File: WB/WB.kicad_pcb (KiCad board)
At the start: 2 copper layers, 89.2 x 84.2 mm, 47 parts, among them J1 Conn_01x04, J2 Conn_01x04, J3 Conn_01x04, J4 Conn_01x04, J5 Pump, J6 Actuator, J7 Actuator, J8 Screw_Terminal_01x02, M1 Fan, Q1 Q_NMOS_GDS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

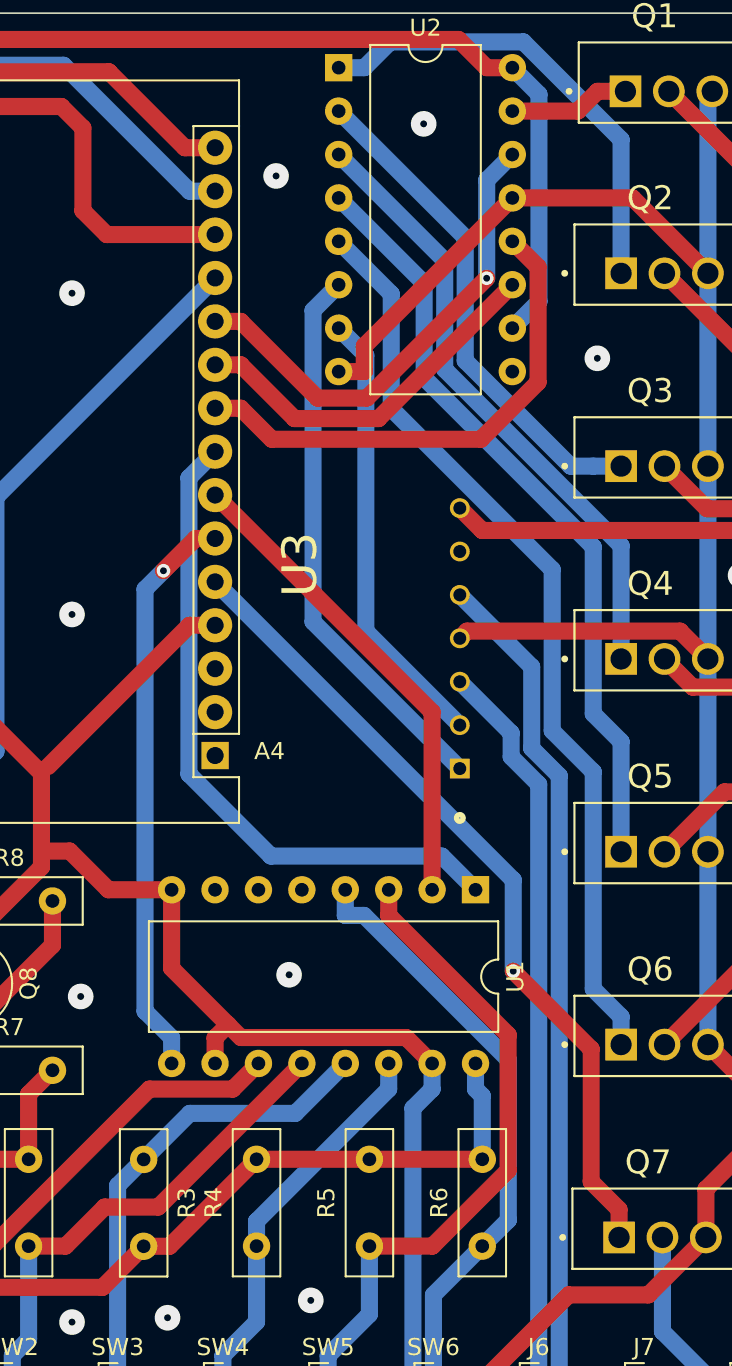
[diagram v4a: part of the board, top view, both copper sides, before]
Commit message: 配線がかぶっていたところを修正
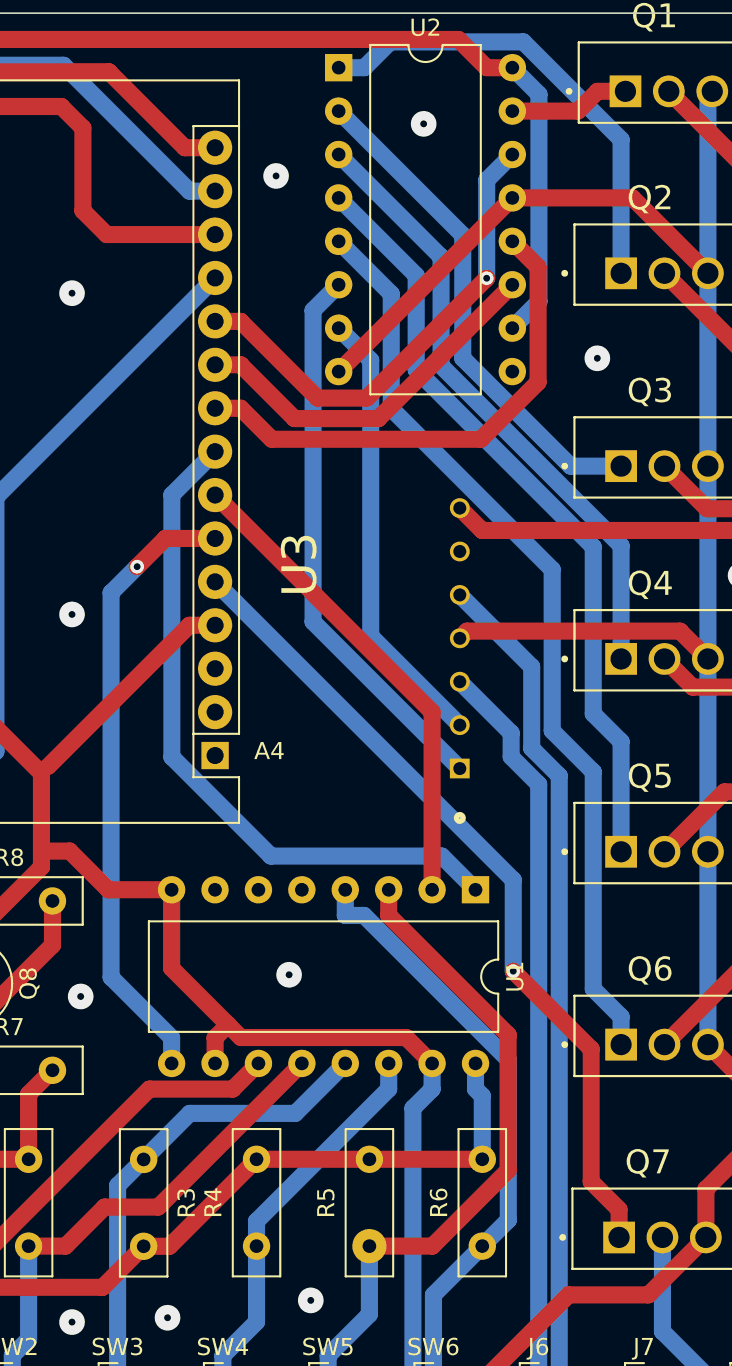
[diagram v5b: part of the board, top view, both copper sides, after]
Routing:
- net Net-(A4-Pad6): track 33.7 -> 36.4 mm
- net GND: track 366.6 -> 365.7 mm
- net Net-(A4-Pad8): track 39.1 -> 39.9 mm
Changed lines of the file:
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@@
     )
     (pad_to_mask_clearance 0)
+    (aux_axis_origin 149.733 106.807)
     (grid_origin 149.733 106.299)
     (pcbplotparams
@@
     (fp_line (start -1.65 1.27) (end 6.73 1.27) (layer "F.Fab") (width 0.1))
     (fp_line (start 6.73 -1.27) (end -1.65 -1.27) (layer "F.Fab") (width 0.1))
-    (pad "1" thru_hole circle (at 0 0 90) (size 1.6 1.6) (drill 0.8) (layers *.Cu *.Mask)
+    (pad "1" thru_hole circle (at 0 0 90) (size 2 2) (drill 0.8) (layers *.Cu *.Mask)
       (net 23 "D4") (pintype "passive"))
     (pad "2" thru_hole circle (at 5.08 0 90) (size 1.6 1.6) (drill 0.8) (layers *.Cu *.Mask)
@@
   (segment (start 192.136 78.4836) (end 192.136 73.894) (width 1) (layer "F.Cu") (net 2))
   (segment (start 219.103 33.416) (end 223.5135 37.8265) (width 1) (layer "F.Cu") (net 2))
-  (segment (start 203.4103 43.576) (end 203.4103 42.0757) (width 1) (layer "F.Cu") (net 2))
   (segment (start 161.0223 82.3434) (end 161.0223 72.2393) (width 1) (layer "F.Cu") (net 2))
   (segment (start 194.676 84.054) (end 194.676 82.5537) (width 1) (layer "F.Cu") (net 2))
@@
   (segment (start 195.4411 81.7886) (end 192.136 78.4836) (width 1) (layer "F.Cu") (net 2))
   (segment (start 227.683 87.122) (end 223.5135 82.9525) (width 1) (layer "F.Cu") (net 2))
-  (segment (start 203.4103 42.0757) (end 212.07 33.416) (width 1) (layer "F.Cu") (net 2))
   (segment (start 194.681 58.42) (end 193.1807 58.42) (width 1) (layer "F.Cu") (net 2))
   (segment (start 195.4411 81.7886) (end 194.676 82.5537) (width 1) (layer "F.Cu") (net 2))
@@
   (segment (start 188.4392 73.894) (end 186.1732 71.628) (width 1) (layer "F.Cu") (net 2))
   (segment (start 192.136 73.894) (end 188.4392 73.894) (width 1) (layer "F.Cu") (net 2))
+  (segment (start 201.91 43.576) (end 212.07 33.416) (width 1) (layer "F.Cu") (net 2))
   (segment (start 159.522 85.344) (end 159.522 83.8437) (width 1) (layer "F.Cu") (net 2))
   (segment (start 188.976 103.617) (end 182.8165 103.617) (width 1) (layer "F.Cu") (net 2))
   (segment (start 207.4545 103.617) (end 209.342 103.617) (width 1) (layer "F.Cu") (net 2))
-  (segment (start 201.91 43.576) (end 203.4103 43.576) (width 1) (layer "F.Cu") (net 2))
   (segment (start 174.2153 103.617) (end 173.7223 103.124) (width 1) (layer "F.Cu") (net 2))
   (segment (start 223.393 94.234) (end 223.393 91.412) (width 1) (layer "F.Cu") (net 2))
@@
   (segment (start 212.07 25.796) (end 213.6289 27.3549) (width 1) (layer "B.Cu") (net 3))
   (segment (start 210.312 85.9503) (end 209.916 85.5543) (width 1) (layer "B.Cu") (net 3))
-  (segment (start 193.1476 49.7934) (end 193.1476 67.1227) (width 1) (layer "B.Cu") (net 4))
-  (segment (start 193.1476 67.1227) (end 197.9473 71.9224) (width 1) (layer "B.Cu") (net 4))
-  (segment (start 194.681 48.26) (end 193.1476 49.7934) (width 1) (layer "B.Cu") (net 4))
+  (segment (start 192.151 50.79) (end 192.151 66.1261) (width 1) (layer "B.Cu") (net 4))
+  (segment (start 192.151 66.1261) (end 197.9473 71.9224) (width 1) (layer "B.Cu") (net 4))
   (segment (start 197.9473 71.9224) (end 207.9444 71.9224) (width 1) (layer "B.Cu") (net 4))
+  (segment (start 194.681 48.26) (end 192.151 50.79) (width 1) (layer "B.Cu") (net 4))
   (segment (start 207.9444 71.9224) (end 209.916 73.894) (width 1) (layer "B.Cu") (net 4))
   (segment (start 207.376 63.495) (end 207.376 73.894) (width 1) (layer "F.Cu") (net 5))
   (segment (start 194.681 50.8) (end 207.376 63.495) (width 1) (layer "F.Cu") (net 5))
-  (segment (start 193.547 53.34) (end 191.6573 55.2297) (width 1) (layer "F.Cu") (net 6))
-  (segment (start 194.681 53.34) (end 193.547 53.34) (width 1) (layer "F.Cu") (net 6))
-  (via (at 191.6573 55.2297) (size 0.8) (drill 0.4) (layers "F.Cu" "B.Cu") (net 6))
-  (segment (start 190.5795 80.9972) (end 190.5795 56.3075) (width 1) (layer "B.Cu") (net 6))
-  (segment (start 190.5795 56.3075) (end 191.6573 55.2297) (width 1) (layer "B.Cu") (net 6))
-  (segment (start 192.136 84.054) (end 192.136 82.5537) (width 1) (layer "B.Cu") (net 6))
-  (segment (start 192.136 82.5537) (end 190.5795 80.9972) (width 1) (layer "B.Cu") (net 6))
+  (segment (start 191.77 53.34) (end 194.681 53.34) (width 1) (layer "F.Cu") (net 6))
+  (segment (start 190.119 54.991) (end 191.77 53.34) (width 1) (layer "F.Cu") (net 6))
+  (via (at 190.119 54.991) (size 0.8) (drill 0.4) (layers "F.Cu" "B.Cu") (net 6))
+  (segment (start 192.136 82.5537) (end 192.136 84.054) (width 1) (layer "B.Cu") (net 6))
+  (segment (start 188.595 56.515) (end 188.595 79.0127) (width 1) (layer "B.Cu") (net 6))
+  (segment (start 188.595 79.0127) (end 192.136 82.5537) (width 1) (layer "B.Cu") (net 6))
+  (segment (start 190.119 54.991) (end 188.595 56.515) (width 1) (layer "B.Cu") (net 6))
   (segment (start 213.614 102.347) (end 219.7735 102.347) (width 1) (layer "F.Cu") (net 7))
   (segment (start 212.002 64.727) (end 212.002 66.1116) (width 1) (layer "B.Cu") (net 7))
@@
   (segment (start 208.997 66.802) (end 200.4096 58.2146) (width 1) (layer "B.Cu") (net 19))
   (segment (start 200.4096 58.2146) (end 200.4096 39.9964) (width 1) (layer "B.Cu") (net 19))
-  (segment (start 203.4984 42.6244) (end 201.91 41.036) (width 1) (layer "B.Cu") (net 20))
-  (segment (start 208.997 64.262) (end 203.4984 58.7634) (width 1) (layer "B.Cu") (net 20))
-  (segment (start 203.4984 58.7634) (end 203.4984 42.6244) (width 1) (layer "B.Cu") (net 20))
+  (segment (start 203.7849 42.9109) (end 201.91 41.036) (width 1) (layer "B.Cu") (net 20))
+  (segment (start 203.7849 59.0499) (end 203.7849 42.9109) (width 1) (layer "B.Cu") (net 20))
+  (segment (start 208.997 64.262) (end 203.7849 59.0499) (width 1) (layer "B.Cu") (net 20))
   (segment (start 211.836 93.218) (end 211.836 83.8367) (width 1) (layer "B.Cu") (net 22))
   (segment (start 207.4545 102.347) (end 207.4545 97.5995) (width 1) (layer "B.Cu") (net 22))
@@
   (segment (start 203.4103 25.796) (end 204.9194 24.2869) (width 1) (layer "B.Cu") (net 30))
   (segment (start 201.91 25.796) (end 203.4103 25.796) (width 1) (layer "B.Cu") (net 30))
-  (segment (start 215.4788 49.108) (end 209.3114 42.9406) (width 1) (layer "B.Cu") (net 31))
-  (segment (start 218.4335 49.108) (end 216.8032 49.108) (width 1) (layer "B.Cu") (net 31))
-  (segment (start 209.3114 35.7374) (end 201.91 28.336) (width 1) (layer "B.Cu") (net 31))
-  (segment (start 216.8032 49.108) (end 215.4788 49.108) (width 1) (layer "B.Cu") (net 31))
-  (segment (start 209.3114 42.9406) (end 209.3114 35.7374) (width 1) (layer "B.Cu") (net 31))
-  (segment (start 208.1111 43.4429) (end 208.1111 37.0771) (width 1) (layer "B.Cu") (net 32))
-  (segment (start 208.1111 37.0771) (end 201.91 30.876) (width 1) (layer "B.Cu") (net 32))
+  (segment (start 209.169 42.7982) (end 209.169 35.595) (width 1) (layer "B.Cu") (net 31))
+  (segment (start 218.4335 49.108) (end 215.4788 49.108) (width 1) (layer "B.Cu") (net 31))
+  (segment (start 209.169 35.595) (end 201.91 28.336) (width 1) (layer "B.Cu") (net 31))
+  (segment (start 215.4788 49.108) (end 209.169 42.7982) (width 1) (layer "B.Cu") (net 31))
   (segment (start 218.4335 60.3895) (end 218.4335 53.7653) (width 1) (layer "B.Cu") (net 32))
-  (segment (start 218.4335 53.7653) (end 208.1111 43.4429) (width 1) (layer "B.Cu") (net 32))
+  (segment (start 207.899 43.2308) (end 207.899 36.865) (width 1) (layer "B.Cu") (net 32))
+  (segment (start 207.899 36.865) (end 201.91 30.876) (width 1) (layer "B.Cu") (net 32))
+  (segment (start 218.4335 53.7653) (end 207.899 43.2308) (width 1) (layer "B.Cu") (net 32))
   (segment (start 175.6787 58.9557) (end 172.222 55.499) (width 1) (layer "B.Cu") (net 33))
   (segment (start 181.8581 50.9229) (end 181.8581 65.8003) (width 1) (layer "B.Cu") (net 33))
@@
   (segment (start 180.208 80.645) (end 181.6583 80.645) (width 1) (layer "F.Cu") (net 35))
   (segment (start 185.166 74.549) (end 185.166 77.1373) (width 1) (layer "F.Cu") (net 35))
-  (segment (start 206.9108 43.9402) (end 206.9108 38.4168) (width 1) (layer "B.Cu") (net 36))
-  (segment (start 206.9108 38.4168) (end 201.91 33.416) (width 1) (layer "B.Cu") (net 36))
+  (segment (start 216.8032 53.8326) (end 206.445 43.4744) (width 1) (layer "B.Cu") (net 36))
+  (segment (start 216.8032 63.5978) (end 216.8032 53.8326) (width 1) (layer "B.Cu") (net 36))
+  (segment (start 206.445 43.4744) (end 206.445 37.951) (width 1) (layer "B.Cu") (net 36))
+  (segment (start 206.445 37.951) (end 201.91 33.416) (width 1) (layer "B.Cu") (net 36))
   (segment (start 218.4335 65.2281) (end 216.8032 63.5978) (width 1) (layer "B.Cu") (net 36))
   (segment (start 218.4335 71.671) (end 218.4335 65.2281) (width 1) (layer "B.Cu") (net 36))
-  (segment (start 216.8032 63.5978) (end 216.8032 53.8326) (width 1) (layer "B.Cu") (net 36))
-  (segment (start 216.8032 53.8326) (end 206.9108 43.9402) (width 1) (layer "B.Cu") (net 36))
   (segment (start 214.4026 55.1566) (end 204.9849 45.7389) (width 1) (layer "B.Cu") (net 37))
   (segment (start 216.8032 79.6919) (end 216.8032 66.9928) (width 1) (layer "B.Cu") (net 37))

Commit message: パッドのサイズを変更したが、だめ
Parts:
- D1, D2, D3, D4, D5, J5, J6, J7, M1, SW1, SW2, SW3, SW4, SW5, SW6: footprint Connector_PinHeader_1.27mm:PinHeader_1x02_P1.27mm_Vertical -> Connector_PinHeader_2.54mm:PinHeader_1x02_P2.54mm_Vertical
- U1, U2: footprint Package_DIP:DIP-16_W10.16mm -> Package_DIP:DIP-16_W7.62mm
- moved SW4 2.42 mm to (194.8, 99.9)
- moved M1 2.40 mm to (225.9, 99.9)
- moved SW6 2.40 mm to (207.5, 99.9)
- moved J6 2.40 mm to (213.6, 99.9)
- moved J7 2.40 mm to (219.8, 99.9)
- moved SW1 2.40 mm to (176.7, 99.9)
- moved SW2 2.40 mm to (182.8, 99.9)
- moved SW3 2.40 mm to (189.0, 99.9)
- moved SW5 2.40 mm to (201.3, 99.9)
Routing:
- net GND: track 365.7 -> 0.00 mm
- net VCC: track 245.7 -> 0.00 mm
- net +24V: track 236.1 -> 0.00 mm
- net Net-(A2-Pad15): track 86.3 -> 0.00 mm
- net Net-(A2-Pad16): track 58.5 -> 0.00 mm
- net Net-(J6-Pad2): track 55.5 -> 0.00 mm
- net Net-(Q6-Pad1): track 53.8 -> 0.00 mm
- net Net-(J6-Pad1): track 48.7 -> 0.00 mm
- net Net-(A4-Pad5): track 48.1 -> 0.00 mm, vias 1 -> 0
- net Net-(Q5-Pad1): track 45.1 -> 0.00 mm
- net Net-(A4-Pad8): track 39.9 -> 0.00 mm
- net D4: track 37.9 -> 0.00 mm
- net Net-(A4-Pad6): track 36.4 -> 0.00 mm, vias 1 -> 0
- net Net-(Q4-Pad1): track 36.4 -> 0.00 mm
- net D5: track 34.9 -> 0.00 mm
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
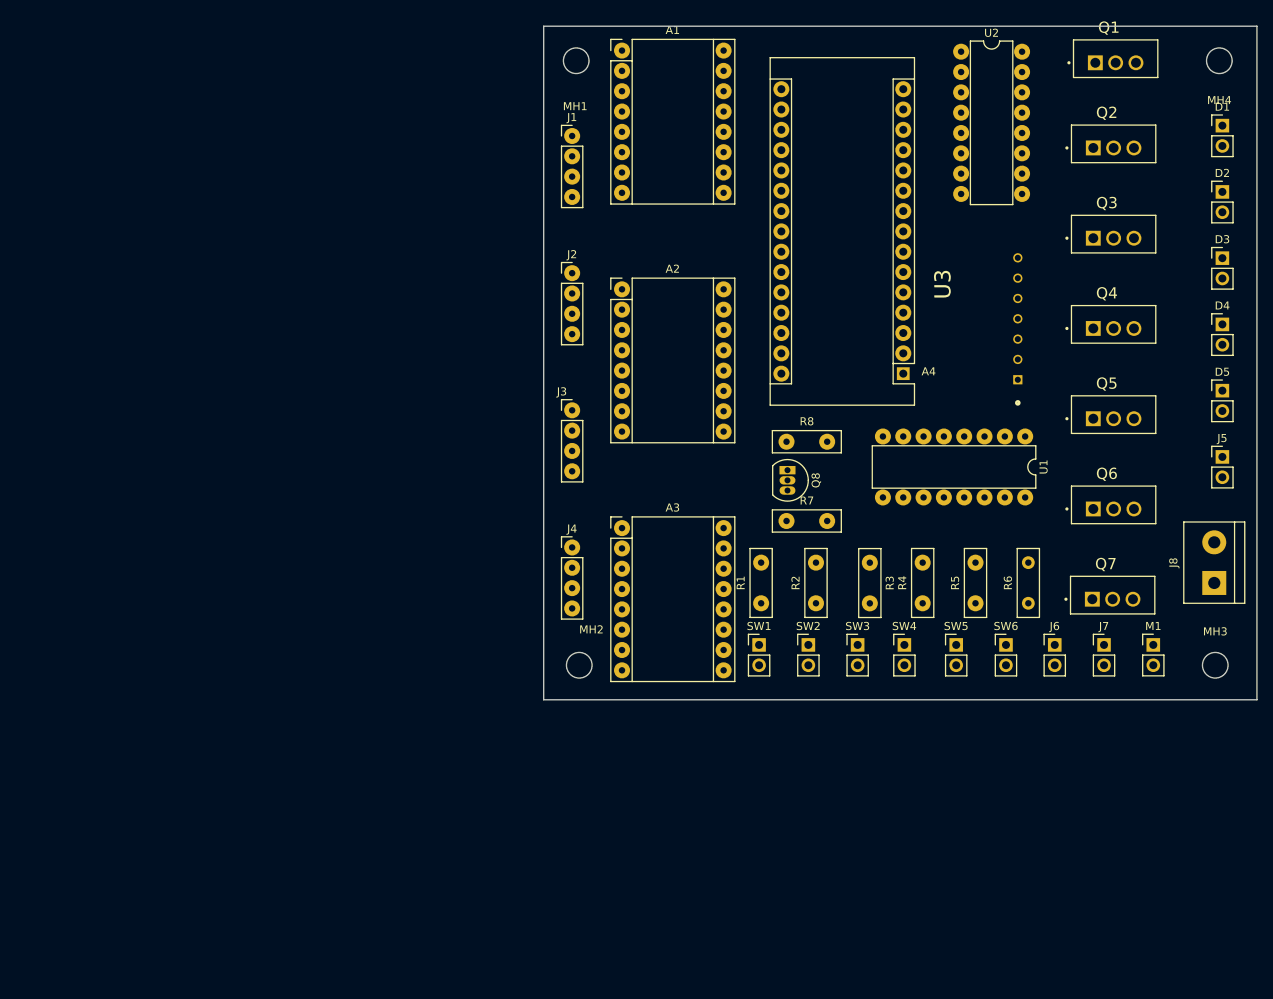
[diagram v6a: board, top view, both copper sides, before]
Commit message: 配線しやすいように回路を変更
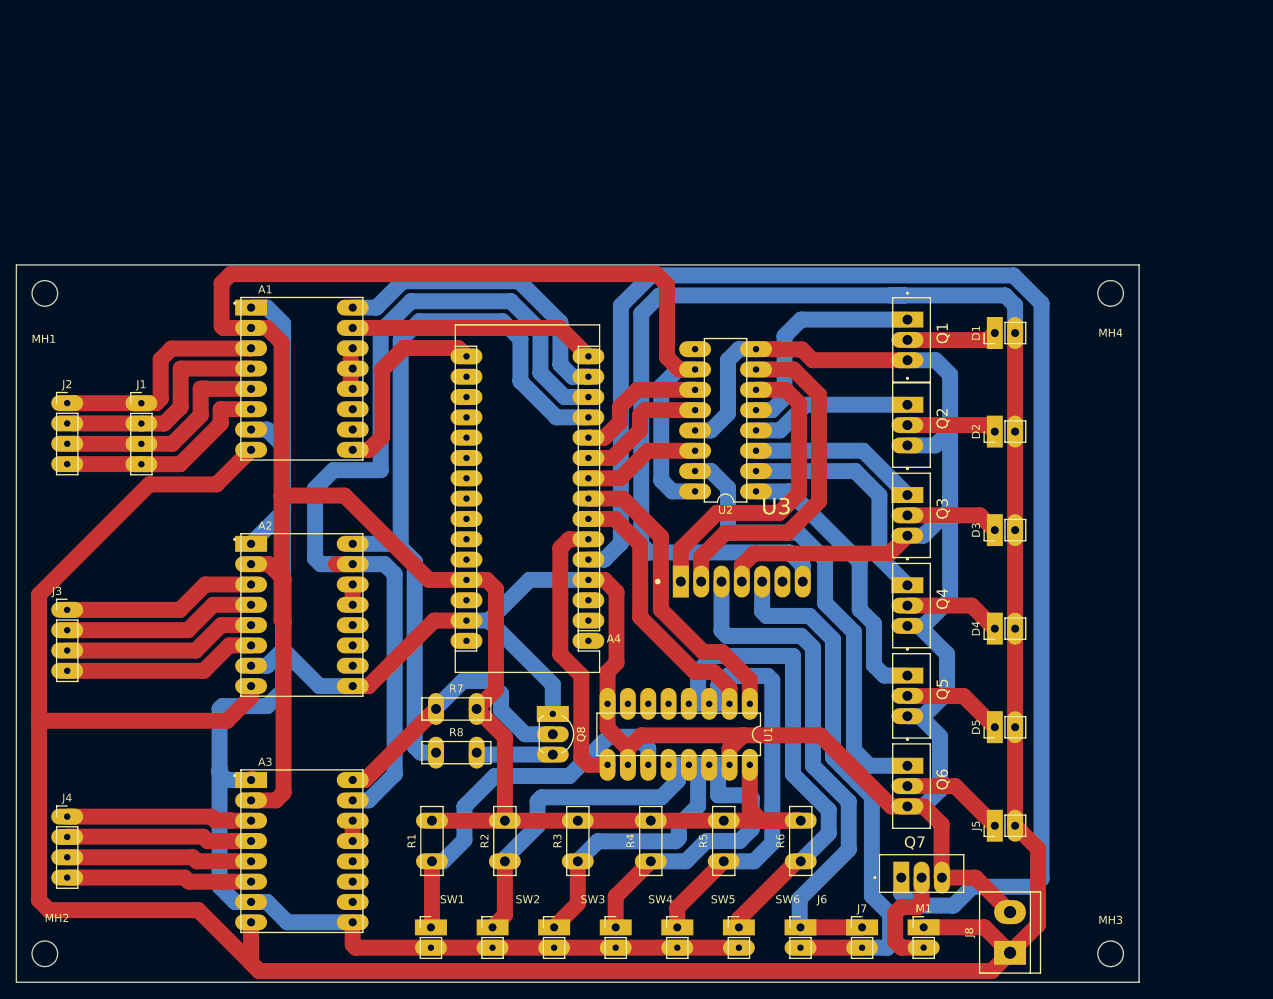
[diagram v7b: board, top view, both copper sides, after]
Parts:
- A1, A2, A3: footprint Module:Pololu_Breakout-16_15.2x20.3mm -> A4988_STEPPER_MOTOR_DRIVER_CARRIER:MODULE_A4988_STEPPER_MOTOR_DRIVER_CARRIER
- Q8: footprint Package_TO_SOT_THT:TO-92_Inline -> Package_TO_SOT_THT:TO-92L_Inline_Wide
- moved MH2 75.9 mm to (87.4, 138.6)
- moved MH1 72.5 mm to (87.4, 56.0)
- moved J4 71.5 mm to (90.2, 121.4)
- moved J3 67.9 mm to (90.2, 95.6)
- moved J2 65.2 mm to (90.2, 69.7)
- moved J1 63.4 mm to (99.4, 69.7)
- moved U2 60.6 mm to (176.3, 80.8), turned to 180 degrees
- moved R8 58.6 mm to (136.3, 113.4)
- moved A1 57.3 mm to (119.5, 66.7)
- moved A2 57.1 mm to (119.5, 96.2)
- moved A3 56.9 mm to (119.5, 125.7)
- moved J5 54.2 mm to (206.1, 122.5), turned to 90 degrees
- moved SW1 54.1 mm to (135.6, 135.3)
- moved SW2 53.0 mm to (143.3, 135.3)
- moved J8 52.8 mm to (208.0, 138.4)
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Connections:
- U2 pad 1: Net-(Q2-Pad1) -> Net-(Q5-Pad1)
- U2 pad 11: Net-(A4-Pad10) -> Net-(A4-Pad11)
- U2 pad 12: Net-(A4-Pad9) -> Net-(A4-Pad10)
- U2 pad 14: Net-(A4-Pad11) -> Net-(A4-Pad9)
- U2 pad 15: Net-(Q1-Pad1) -> Net-(Q6-Pad1)
- U2 pad 2: Net-(Q3-Pad1) -> Net-(Q4-Pad1)
- U2 pad 3: Net-(Q4-Pad1) -> Net-(Q3-Pad1)
- U2 pad 4: Net-(Q5-Pad1) -> Net-(Q2-Pad1)
- U2 pad 5: Net-(Q6-Pad1) -> Net-(Q1-Pad1)
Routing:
- net GND: track 0.00 -> 477.1 mm
- net +24V: track 0.00 -> 431.6 mm
- net VCC: track 0.00 -> 297.7 mm
- net Net-(A4-Pad5): track 0.00 -> 183.6 mm
- net Net-(A2-Pad15): track 0.00 -> 115.3 mm
- net Net-(A2-Pad16): track 0.00 -> 95.7 mm
- net Net-(J6-Pad2): track 0.00 -> 66.6 mm
- net Net-(J6-Pad1): track 0.00 -> 65.5 mm
- net D5: track 0.00 -> 56.9 mm
- net Net-(Q6-Pad1): track 0.00 -> 56.6 mm
- net D4: track 0.00 -> 47.8 mm
- net D0: track 0.00 -> 46.9 mm
- net Net-(U2-Pad7): track 0.00 -> 43.2 mm
- net Net-(U2-Pad6): track 0.00 -> 39.1 mm
- net Net-(A1-Pad16): track 0.00 -> 38.9 mm
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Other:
- board size 89.2 x 84.2 mm -> 140.3 x 89.7 mm
- board text removed: "Made by Ruchi"
